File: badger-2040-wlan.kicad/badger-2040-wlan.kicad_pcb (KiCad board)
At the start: 2 copper layers, 42 x 40.1 mm, 6 parts, among them U1 Badger2040_Conn, U3 SN74LVC1G14DBV, U4 ESP_01S_Breakout, U5 PCF8523_RTC_Breakouut

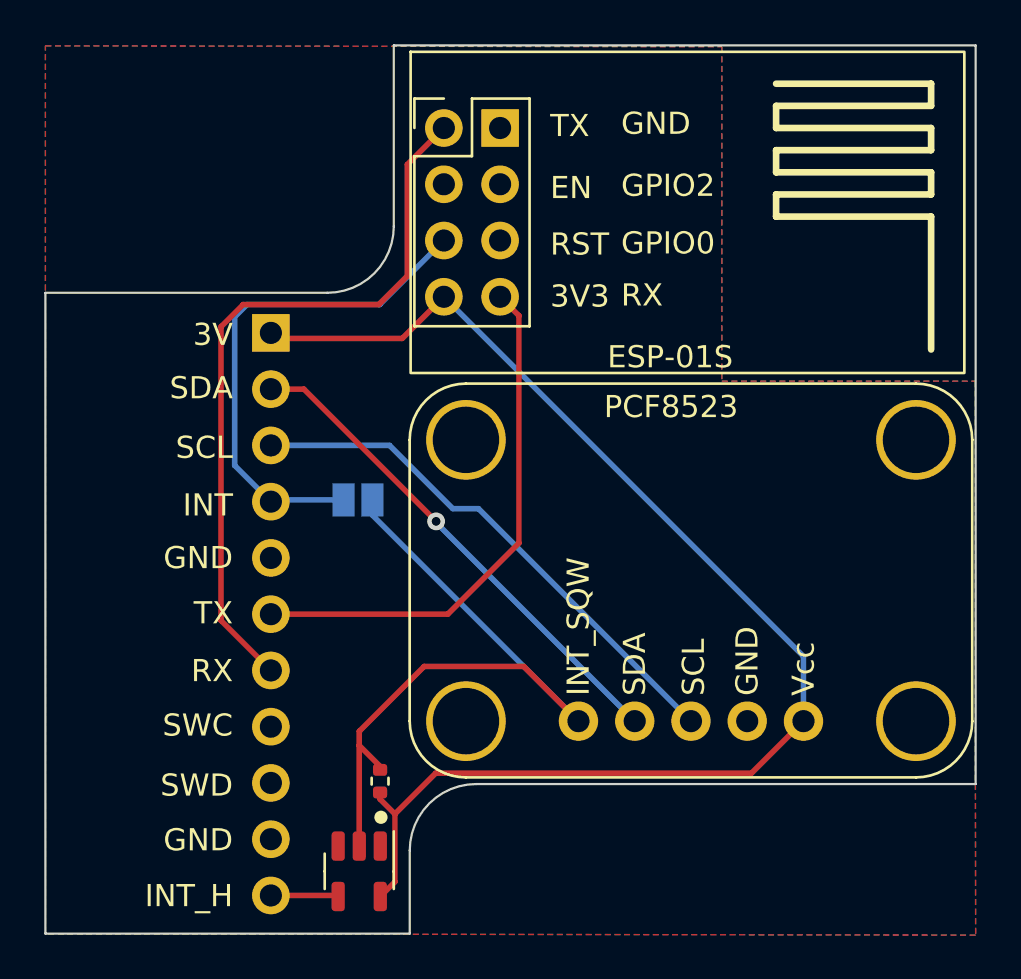
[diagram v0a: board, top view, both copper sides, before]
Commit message: Rev 4: removed pullup and inverter for RTC (INT_SQW)
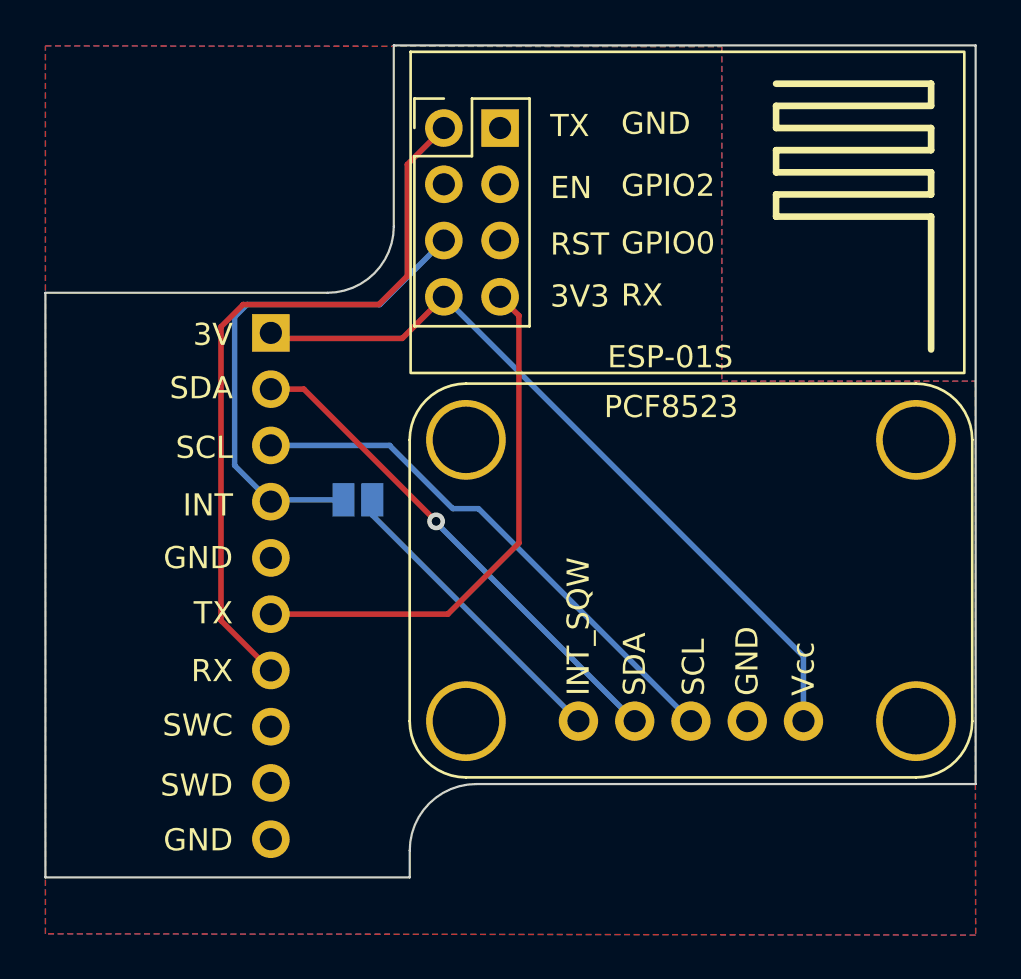
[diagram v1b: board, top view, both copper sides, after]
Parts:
- removed R1: 100K, Resistor_SMD:R_0402_1005Metric
- removed U3: SN74LVC1G14DBV, Package_TO_SOT_SMD:SOT-23-5
- U1: footprint user:PinSocket_1x11_P2.54mm_Horizontal_Back -> user:PinSocket_1x10_P2.54mm_Horizontal_Back
- U5: value PCF8523_RTC_Breakouut -> PCF8523_RTC_Breakout
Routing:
- net +3V3: track 60.0 -> 34.6 mm
- net Net-(JP1-Pad1): track 32.7 -> 13.8 mm
- net Net-(U1-Pad11): track 3.06 -> 0.00 mm
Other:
- board size 42 x 40.1 mm -> 42 x 37.6 mm
- board text added: "https://github.com/bablokb/ badger-2040-wlan Rev 4"
- board text removed: "INT_H"
- board text removed: "https://github.com/bablokb/ badger-2040-wlan Rev 3"
